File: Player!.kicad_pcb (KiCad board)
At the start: 2 copper layers, 95.2 x 38.1 mm, 25 parts, among them J1 USB4085-GF-A_REVA4, SW1 SW_Push, SW2 SW_Push, SW3 SW_Push, SW4 SW_Push, SW5 RotaryEncoder_Switch

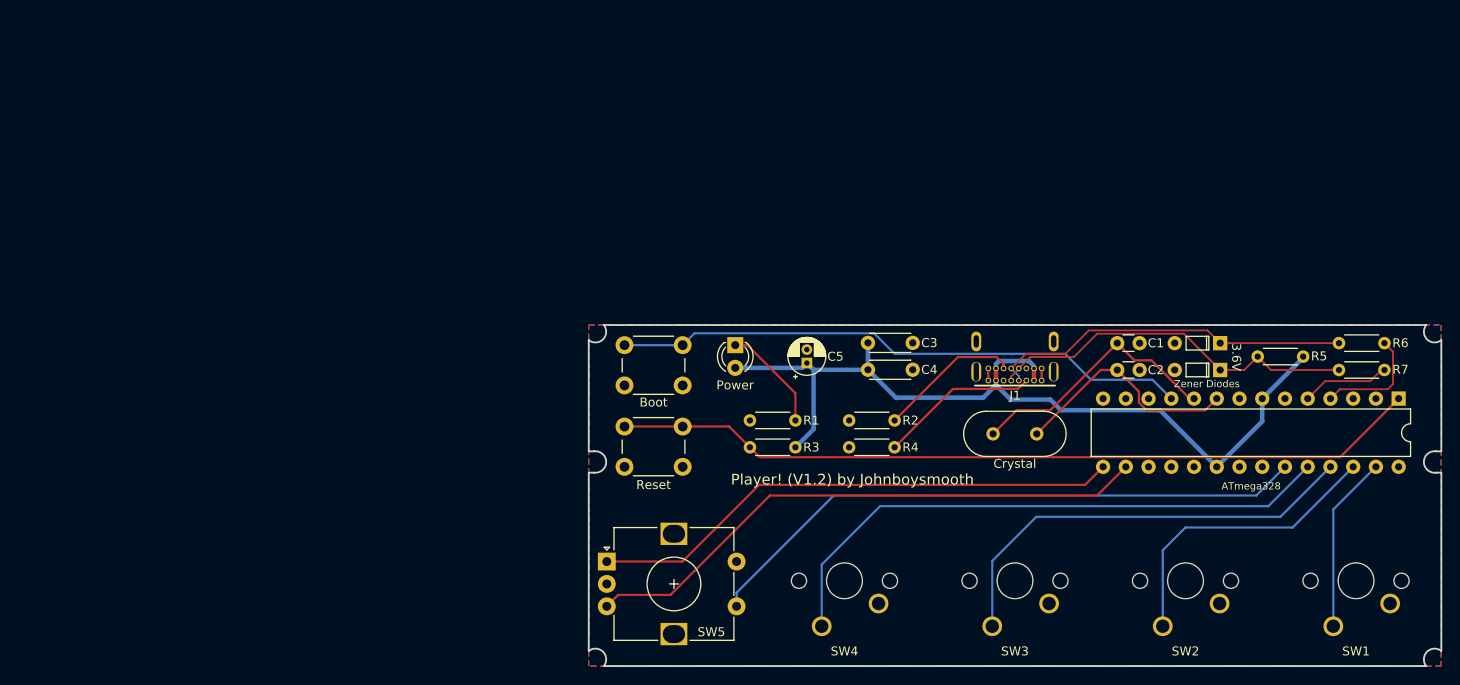
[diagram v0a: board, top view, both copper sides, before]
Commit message: Updated to V1.31
V1.31 makes the bigger to accommodate 4 mounting holes, adds a decorative tropical pattern to the top copper plane in the otherwise blank space; numerous small changes made to improve the overall appearance. Some changes were made to footprints and their silkscreens, as well as move their reference point. Switched to Kailh hotswap sockets for the switches.
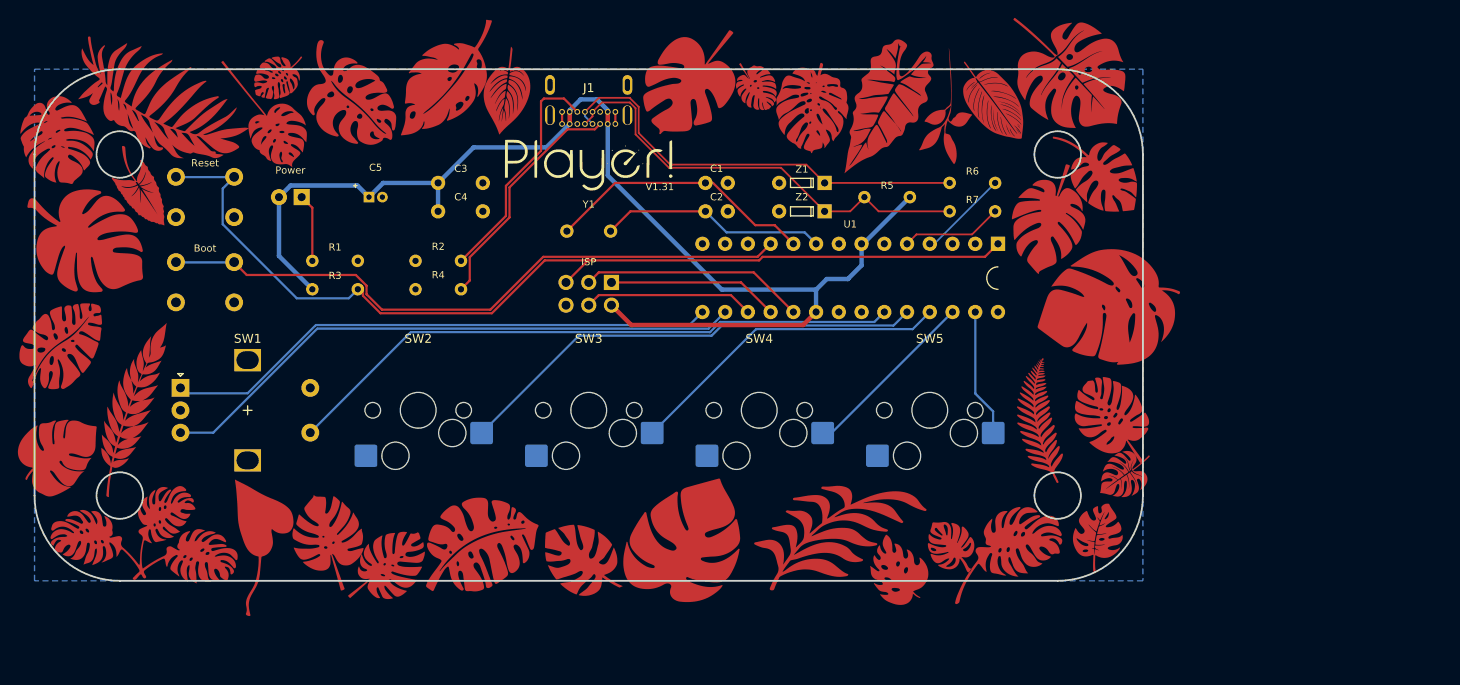
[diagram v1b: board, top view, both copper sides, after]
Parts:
- added J2: ISP, Keyboard Stuff:PinHeader_2x03_P2.54mm_Vertical, F.Cu at (0.00, -3.49)
- D1: renamed from Power; value POWERLED -> Power
- R7: footprint Resistor_THT:R_Axial_DIN0204_L3.6mm_D1.6mm_P5.08mm_Horizontal -> Keyboard Stuff:R_Axial_DIN0204_L3.6mm_D1.6mm_P5.08mm_Horizontal
- SW2, SW3, SW4: footprint Keyboard Stuff:Player! 1u PCB -> Keyboard Stuff:SW_Hotswap_Kailh_MX_1.00u
- SW5: renamed from SW1; footprint Keyboard Stuff:Player! 1u PCB -> Keyboard Stuff:SW_Hotswap_Kailh_MX_1.00u
- SW6: renamed from Reset; value RESET -> Reset
- SW7: renamed from Boot; value BOOT -> Boot
- moved SW2 86.6 mm to (-19.1, 9.53)
- moved U1 62.7 mm to (29.2, -5.26)
- moved J1 55.6 mm to (0.00, -26.5)
- moved R1 54.4 mm to (-28.3, -7.17)
- moved R3 54.4 mm to (-28.3, -3.99)
- moved R2 54.0 mm to (-16.8, -7.17), turned to 0 degrees
- moved R4 53.9 mm to (-16.8, -3.99), turned to 0 degrees
- moved SW6 53.4 mm to (-42.9, -14.3), turned to 180 degrees
- moved D1 52.4 mm to (-33.3, -14.3)
- moved C5 51.6 mm to (-23.8, -14.3)
- moved SW5 51.1 mm to (38.1, 9.53)
- moved SW3 51.1 mm to (0.00, 9.53)
- moved Y1 50.5 mm to (0.00, -10.5)
- moved Z1 50.0 mm to (23.8, -15.9)
- moved Z2 50.0 mm to (23.8, -12.7)
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- renumbered SW5 to SW1, ATmega328 to U1, Crystal1 to Y1, DN1 to Z1, DP1 to Z2
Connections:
- C1 pad 1: /XTAL2 -> XTAL1
- C2 pad 1: /XTAL1 -> XTAL2
- J1 pad A6: /DP -> /DN
- J1 pad B6: /DP -> /DN
- R3 pad 2: /RST -> RST
- R6 pad 1: /DP -> /DN
- SW1 pad S2: SW5 -> SW1
- SW5 pad 1: SW1 -> SW5
- SW6 pad 1: /RST -> GND
- SW6 pad 2: GND -> RST
- SW7 pad 1: /BOOT -> GND
- SW7 pad 2: GND -> BOOT
- U1 pad 1: /RST -> RST
- U1 pad 10: /XTAL2 -> XTAL2
- U1 pad 11: /BOOT -> BOOT
- U1 pad 17: unconnected-(ATMega328-Pad17) -> MOSI
- U1 pad 18: unconnected-(ATMega328-Pad18) -> MISO
- U1 pad 19: unconnected-(ATMega328-Pad19) -> SCK
- U1 pad 23: SW5 -> SW1
- U1 pad 24: SW4 -> SW2
- U1 pad 26: SW2 -> SW4
- U1 pad 27: SW1 -> SW5
- U1 pad 9: /XTAL1 -> XTAL1
- Y1 pad 1: /XTAL2 -> XTAL1
- Y1 pad 2: /XTAL1 -> XTAL2
- Z1 pad 1: /DP -> /DN
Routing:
- net RST: track 0.00 -> 111.7 mm
- net /RST: track 90.6 -> 0.00 mm
- net BOOT: track 0.00 -> 72.2 mm
- net /BOOT: track 64.7 -> 0.00 mm
- net /DN: track 41.6 -> 98.9 mm
- net SW5: track 68.6 -> 14.3 mm
- net SW1: track 19.8 -> 69.7 mm
- net SW4: track 65.7 -> 20.1 mm
- net /DP: track 40.3 -> 0.00 mm
- net +5V: track 97.4 -> 137.7 mm
- net XTAL1: track 0.00 -> 30.3 mm
- net /XTAL2: track 29.2 -> 0.00 mm
- net /XTAL1: track 26.2 -> 0.00 mm
- net XTAL2: track 0.00 -> 25.4 mm
- net SCK: track 0.00 -> 25.2 mm
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- removed copper zone on F.Cu, net GND
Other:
- board size 95.2 x 38.1 mm -> 123.8 x 57.1 mm
- board text added: "Designed by Johnboysmooth South Yorkshire, UK 06-2023"
- board text added: "V1.31"
- board text removed: "3.6V"
- board text removed: "Player! (V1.2) by Johnboysmooth"
- board text removed: "Zener Diodes"

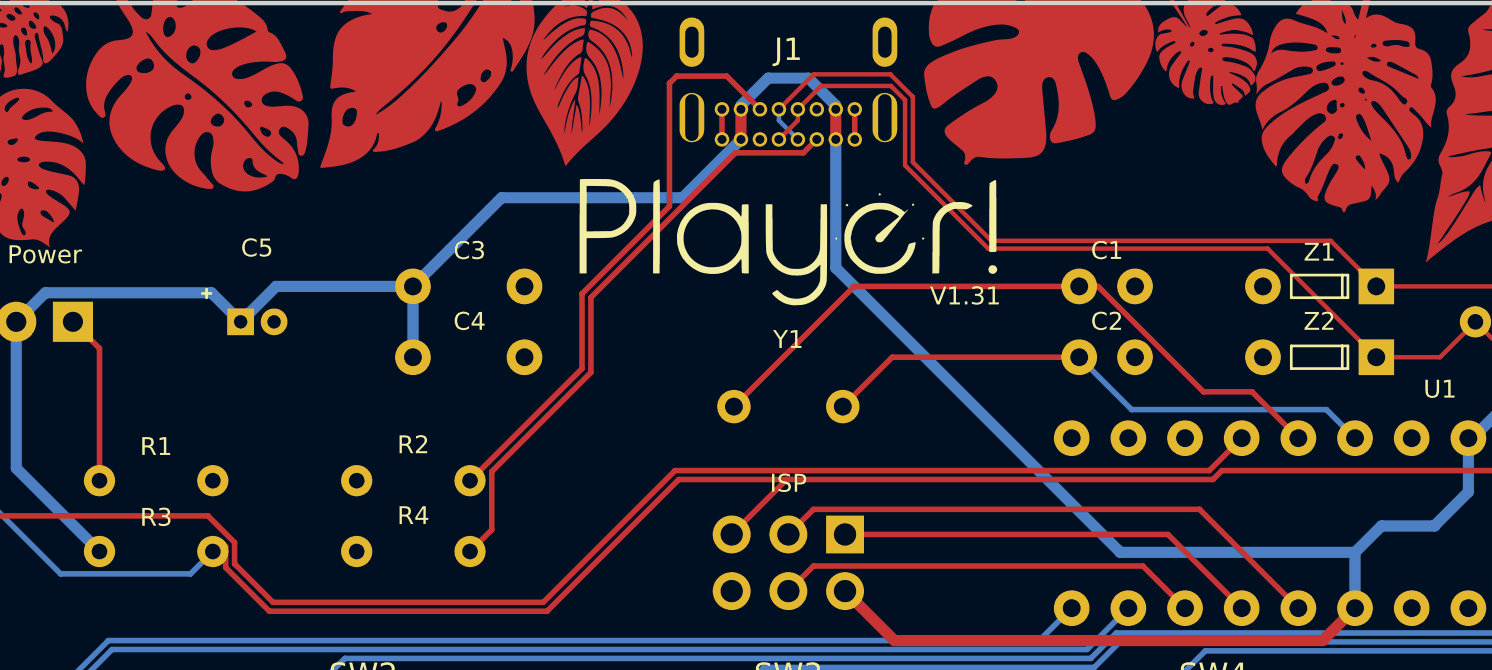
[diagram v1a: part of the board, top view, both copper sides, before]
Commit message: PCB changes
Minor changes to correct D+ & D- tracks connecting
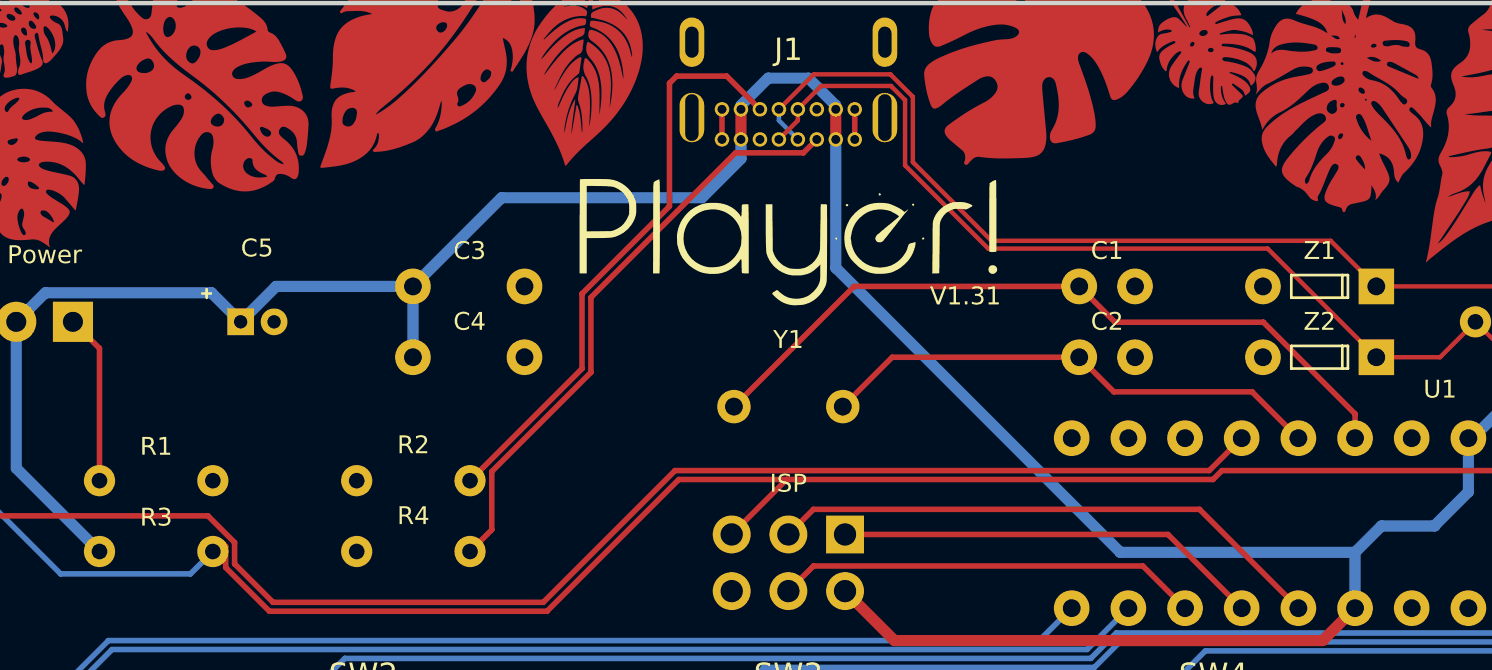
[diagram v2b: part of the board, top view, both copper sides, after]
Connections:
- J1 pad A6: /DN -> /DP
- J1 pad B6: /DN -> /DP
- R6 pad 1: /DN -> /DP
- Z1 pad 1: /DN -> /DP
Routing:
- net /DN: track 98.9 -> 50.1 mm
- net /DP: track 0.00 -> 48.8 mm
- net XTAL1: track 30.3 -> 33.5 mm
- net XTAL2: track 25.4 -> 22.8 mm
- net +5V: track 137.7 -> 138.2 mm

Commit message: Final PCB changes for v1.31
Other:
- board text added: "Designed by Johnboysmooth South Yorkshire, UK 07-2023"
- board text removed: "Designed by Johnboysmooth South Yorkshire, UK 06-2023"
